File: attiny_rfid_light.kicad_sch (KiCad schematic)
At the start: 27 parts, among them IC1 EM4095, U1 ESP32-WROOM-32, U2 NCP1117-3.3_SOT223

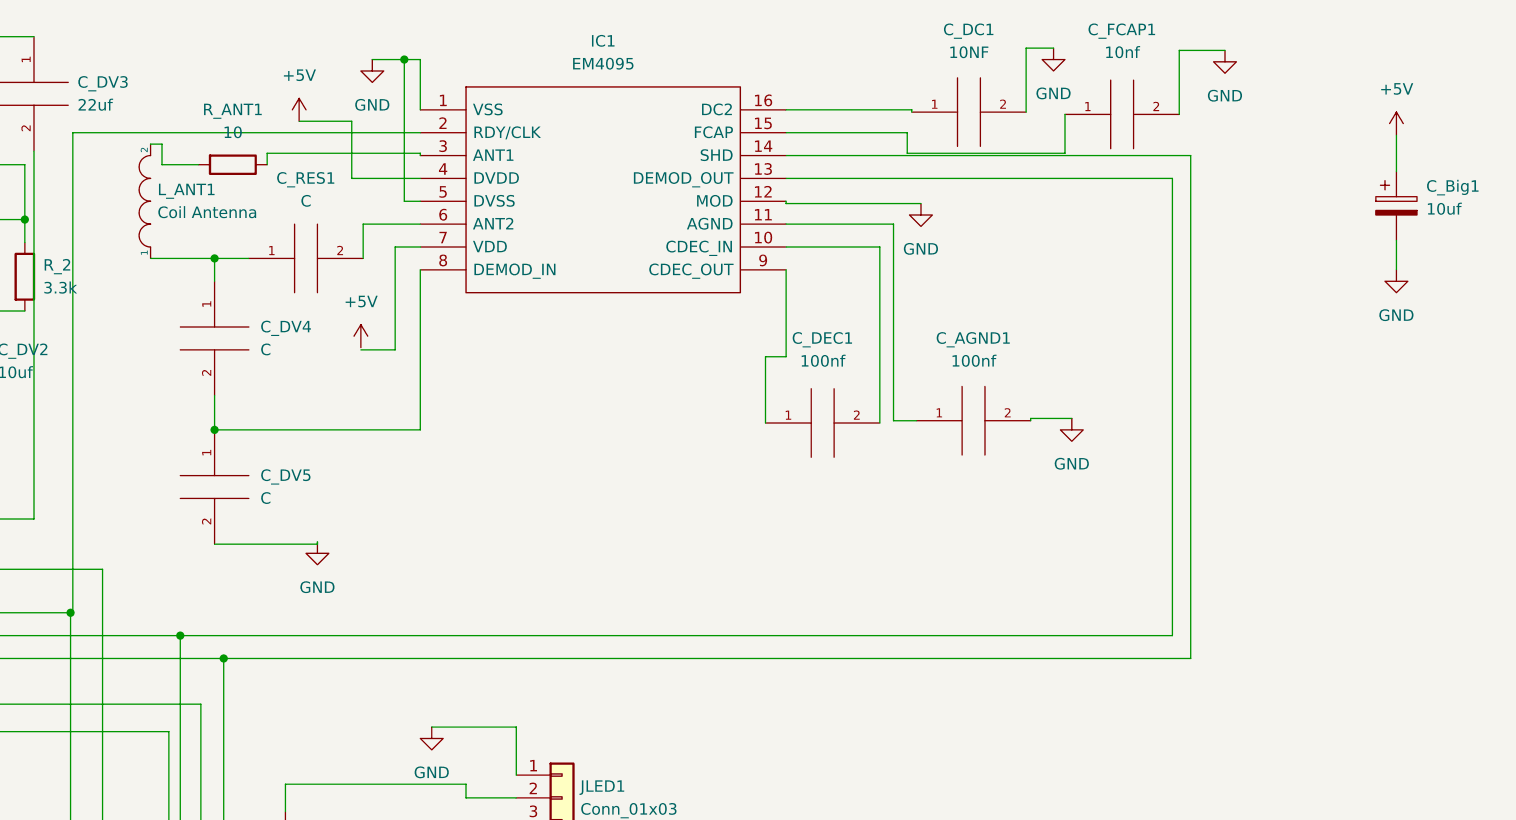
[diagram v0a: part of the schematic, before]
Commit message: Update fix antenna direction and missing shd trace
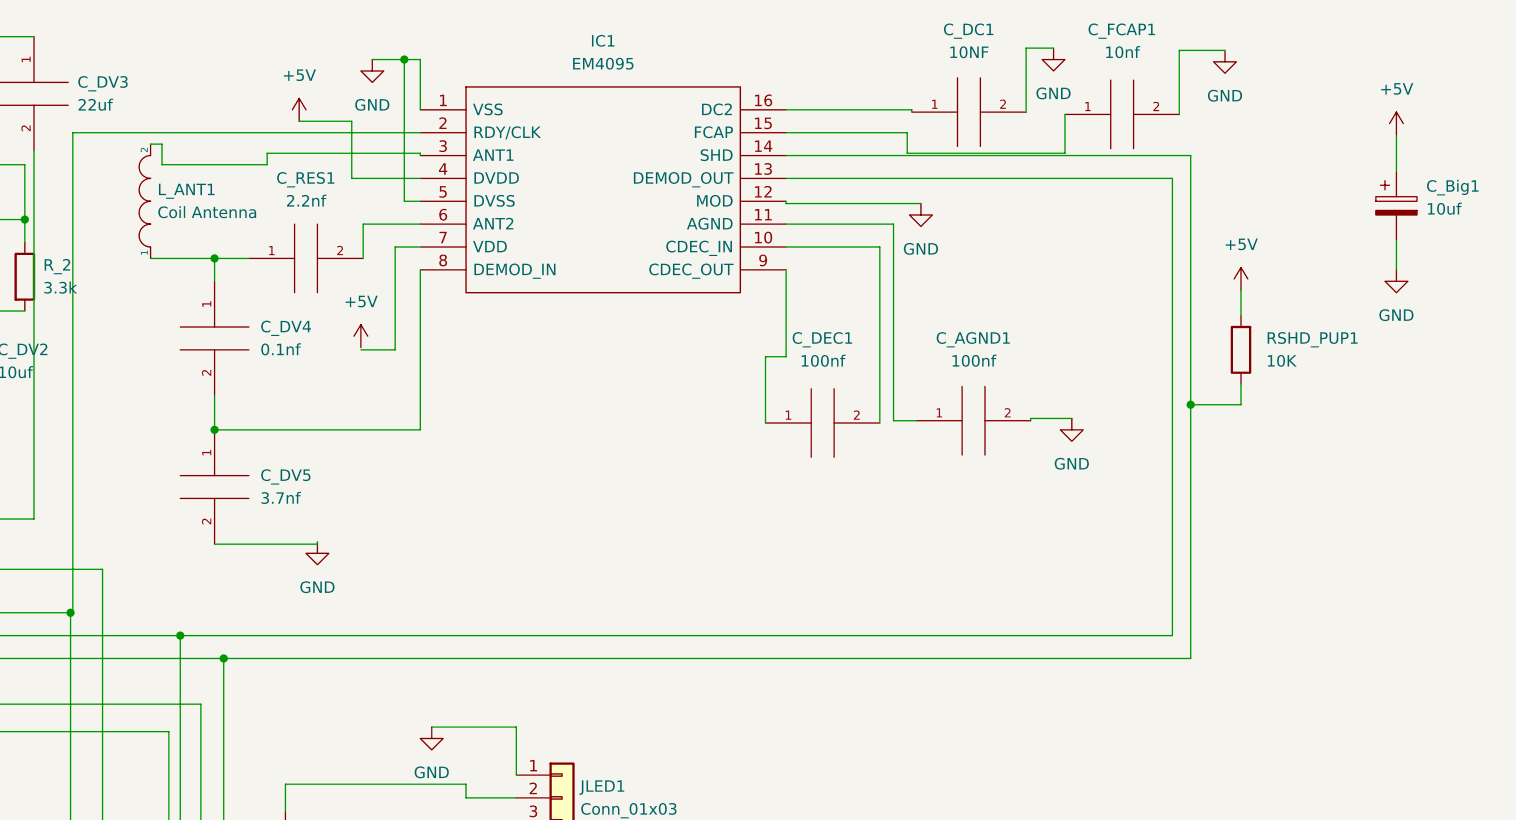
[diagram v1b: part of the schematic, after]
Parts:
- removed R_ANT1: 10, Resistor_SMD:R_0805_2012Metric_Pad1.20x1.40mm_HandSolder, symbol Device:R
- added RSHD_PUP1: 10K, Resistor_SMD:R_0805_2012Metric_Pad1.20x1.40mm_HandSolder, symbol Device:R
- C_DV4: value C -> 0.1nf
- C_DV5: value C -> 3.7nf
- C_RES1: value C -> 2.2nf
- L_ANT1: footprint pcb_inductors:60_turn_square_inductor -> pcb_inductors:60_turn_square_inductor_corrected
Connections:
- net +5V: now also RSHD_PUP1.2
- net at IC1.14 (SHD), J_DEBUG1.4 (Pin_4), U1.26 (IO4): now also RSHD_PUP1.1
- net at IC1.3 (ANT1): now also L_ANT1.2
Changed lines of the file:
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@@
   (junction (at 90.17 80.01) (diameter 0) (color 0 0 0 0)
   )
+  (junction (at 202.438 54.356) (diameter 0) (color 0 0 0 0)
+  )
   (junction (at 59.436 41.402) (diameter 0) (color 0 0 0 0)
   )
@@
     (stroke (width 0) (type default) (color 0 0 0 0))
   )
+  (wire (pts (xy 208.026 41.656) (xy 208.026 44.45))
+    (stroke (width 0) (type default) (color 0 0 0 0))
+  )
   (wire (pts (xy 170.942 26.416) (xy 188.468 26.416))
     (stroke (width 0) (type default) (color 0 0 0 0))
@@
     (stroke (width 0) (type default) (color 0 0 0 0))
   )
+  (wire (pts (xy 208.026 54.356) (xy 202.438 54.356))
+    (stroke (width 0) (type default) (color 0 0 0 0))
+  )
   (wire (pts (xy 116.84 26.416) (xy 116.84 26.67))
     (stroke (width 0) (type default) (color 0 0 0 0))
@@
     (stroke (width 0) (type default) (color 0 0 0 0))
   )
+  (wire (pts (xy 202.438 54.356) (xy 202.438 26.67))
+    (stroke (width 0) (type default) (color 0 0 0 0))
+  )
   (wire (pts (xy 121.92 98.044) (xy 127.508 98.044))
     (stroke (width 0) (type default) (color 0 0 0 0))
@@
     (stroke (width 0) (type default) (color 0 0 0 0))
   )
-  (wire (pts (xy 92.202 27.686) (xy 88.138 27.686))
+  (wire (pts (xy 208.026 52.07) (xy 208.026 54.356))
+    (stroke (width 0) (type default) (color 0 0 0 0))
+  )
+  (wire (pts (xy 88.138 27.686) (xy 99.822 27.686))
     (stroke (width 0) (type default) (color 0 0 0 0))
   )
@@
     (stroke (width 0) (type default) (color 0 0 0 0))
   )
-  (wire (pts (xy 202.438 82.55) (xy 202.438 26.67))
+  (wire (pts (xy 202.438 82.55) (xy 202.438 54.356))
     (stroke (width 0) (type default) (color 0 0 0 0))
   )
@@
       (effects (font (size 1.27 1.27)) (justify left))
     )
-    (property "Value" "C" (id 1) (at 99.06 64.7699 0)
+    (property "Value" "3.7nf" (id 1) (at 99.06 64.7699 0)
       (effects (font (size 1.27 1.27)) (justify left))
     )
@@
   (symbol (lib_id "power:+5V") (at 225.298 24.384 0) (unit 1)
     (in_bom yes) (on_board yes) (fields_autoplaced)
-    (property "Reference" "#PWR019" (id 0) (at 225.298 28.194 0)
+    (property "Reference" "#PWR020" (id 0) (at 225.298 28.194 0)
       (effects (font (size 1.27 1.27)) hide)
     )
@@
     )
     (pin "1")
-  )
-  (symbol (lib_id "Device:R") (at 96.012 27.686 270) (unit 1)
-    (in_bom yes) (on_board yes) (fields_autoplaced)
-    (property "Reference" "R_ANT1" (id 0) (at 96.012 21.59 90))
-    (property "Value" "10" (id 1) (at 96.012 24.13 90))
-    (property "Footprint" "Resistor_SMD:R_0805_2012Metric_Pad1.20x1.40mm_HandSolder" (id 2) (at 96.012 25.908 90)
-      (effects (font (size 1.27 1.27)) hide)
-    )
-    (property "Datasheet" "~" (id 3) (at 96.012 27.686 0)
-      (effects (font (size 1.27 1.27)) hide)
-    )
-    (pin "1")
-    (pin "2")
   )
   (symbol (lib_id "power:GND") (at 118.11 90.17 0) (unit 1)
@@
     (pin "1")
   )
+  (symbol (lib_id "Device:R") (at 208.026 48.26 180) (unit 1)
+    (in_bom yes) (on_board yes) (fields_autoplaced)
+    (property "Reference" "RSHD_PUP1" (id 0) (at 210.82 46.9899 0)
+      (effects (font (size 1.27 1.27)) (justify right))
+    )
+    (property "Value" "10K" (id 1) (at 210.82 49.5299 0)
+      (effects (font (size 1.27 1.27)) (justify right))
+    )
+    (property "Footprint" "Resistor_SMD:R_0805_2012Metric_Pad1.20x1.40mm_HandSolder" (id 2) (at 209.804 48.26 90)
+      (effects (font (size 1.27 1.27)) hide)
+    )
+    (property "Datasheet" "~" (id 3) (at 208.026 48.26 0)
+      (effects (font (size 1.27 1.27)) hide)
+    )
+    (pin "1")
+    (pin "2")
+  )
   (symbol (lib_id "power:GND") (at 172.466 32.004 0) (unit 1)
     (in_bom yes) (on_board yes) (fields_autoplaced)
@@
       (effects (font (size 1.27 1.27)) (justify left))
     )
-    (property "Value" "C" (id 1) (at 99.06 48.2599 0)
+    (property "Value" "0.1nf" (id 1) (at 99.06 48.2599 0)
       (effects (font (size 1.27 1.27)) (justify left))
     )
@@
   (symbol (lib_id "power:GND") (at 225.298 39.37 0) (unit 1)
     (in_bom yes) (on_board yes) (fields_autoplaced)
-    (property "Reference" "#PWR020" (id 0) (at 225.298 45.72 0)
+    (property "Reference" "#PWR021" (id 0) (at 225.298 45.72 0)
       (effects (font (size 1.27 1.27)) hide)
     )
@@
     (pin "1")
   )
+  (symbol (lib_id "power:+5V") (at 208.026 41.656 0) (unit 1)
+    (in_bom yes) (on_board yes) (fields_autoplaced)
+    (property "Reference" "#PWR019" (id 0) (at 208.026 45.466 0)
+      (effects (font (size 1.27 1.27)) hide)
+    )
+    (property "Value" "+5V" (id 1) (at 208.026 36.576 0))
+    (property "Footprint" "" (id 2) (at 208.026 41.656 0)
+      (effects (font (size 1.27 1.27)) hide)
+    )
+    (property "Datasheet" "" (id 3) (at 208.026 41.656 0)
+      (effects (font (size 1.27 1.27)) hide)
+    )
+    (pin "1")
+  )
   (symbol (lib_id "pspice:C") (at 47.498 40.386 0) (unit 1)
     (in_bom yes) (on_board yes) (fields_autoplaced)
@@
       (effects (font (size 1.27 1.27)) (justify right))
     )
-    (property "Footprint" "pcb_inductors:60_turn_square_inductor" (id 2) (at 86.868 31.75 0)
+    (property "Footprint" "pcb_inductors:60_turn_square_inductor_corrected" (id 2) (at 86.868 31.75 0)
       (effects (font (size 1.27 1.27)) hide)
     )
@@
     (in_bom yes) (on_board yes) (fields_autoplaced)
     (property "Reference" "C_RES1" (id 0) (at 104.14 29.21 90))
-    (property "Value" "C" (id 1) (at 104.14 31.75 90))
+    (property "Value" "2.2nf" (id 1) (at 104.14 31.75 90))
     (property "Footprint" "Capacitor_SMD:C_0805_2012Metric_Pad1.18x1.45mm_HandSolder" (id 2) (at 104.14 38.1 0)
       (effects (font (size 1.27 1.27)) hide)
@@
       (reference "#PWR018") (unit 1) (value "GND") (footprint "")
     )
+    (path "/b85b5a44-5181-4c70-bb4d-8740fed21aeb"
+      (reference "#PWR019") (unit 1) (value "+5V") (footprint "")
+    )
     (path "/160fdae6-4399-4d83-be6f-257342eb6a1a"
-      (reference "#PWR019") (unit 1) (value "+5V") (footprint "")
+      (reference "#PWR020") (unit 1) (value "+5V") (footprint "")
     )
     (path "/9ce4a190-6d15-4275-9160-36acf534b781"
-      (reference "#PWR020") (unit 1) (value "GND") (footprint "")
+      (reference "#PWR021") (unit 1) (value "GND") (footprint "")
     )
     (path "/fc3bfa78-5d04-417d-b08f-768062b2f9aa"
@@
     )
     (path "/88f84baf-7afe-41aa-824c-29b1057bce53"
-      (reference "C_DV4") (unit 1) (value "C") (footprint "Capacitor_SMD:C_0805_2012Metric_Pad1.18x1.45mm_HandSolder")
+      (reference "C_DV4") (unit 1) (value "0.1nf") (footprint "Capacitor_SMD:C_0805_2012Metric_Pad1.18x1.45mm_HandSolder")
     )
     (path "/0970727f-11dd-473f-b585-f40294eee11b"
-      (reference "C_DV5") (unit 1) (value "C") (footprint "Capacitor_SMD:C_0805_2012Metric_Pad1.18x1.45mm_HandSolder")
+      (reference "C_DV5") (unit 1) (value "3.7nf") (footprint "Capacitor_SMD:C_0805_2012Metric_Pad1.18x1.45mm_HandSolder")
     )
     (path "/5fade6ac-277b-43df-8e3a-ea7ae9efe0a9"
@@
     )
     (path "/eb36eec3-209f-45cf-a105-18a7e7672fef"
-      (reference "C_RES1") (unit 1) (value "C") (footprint "Capacitor_SMD:C_0805_2012Metric_Pad1.18x1.45mm_HandSolder")
+      (reference "C_RES1") (unit 1) (value "2.2nf") (footprint "Capacitor_SMD:C_0805_2012Metric_Pad1.18x1.45mm_HandSolder")
     )
     (path "/72ff0485-f700-4243-a66c-13414af86c8f"
@@
     )
     (path "/c4f366cf-8726-47ee-87f5-b5abbd410713"
-      (reference "L_ANT1") (unit 1) (value "Coil Antenna") (footprint "pcb_inductors:60_turn_square_inductor")
+      (reference "L_ANT1") (unit 1) (value "Coil Antenna") (footprint "pcb_inductors:60_turn_square_inductor_corrected")
+    )
+    (path "/81c65984-9f9d-492c-82f9-bbe24b88ebc2"
+      (reference "RSHD_PUP1") (unit 1) (value "10K") (footprint "Resistor_SMD:R_0805_2012Metric_Pad1.20x1.40mm_HandSolder")
     )
     (path "/b2b8605e-6475-43cb-8fde-09cbdf493df9"
@@
       (reference "R_5") (unit 1) (value "490") (footprint "Resistor_SMD:R_0805_2012Metric_Pad1.20x1.40mm_HandSolder")
     )
-    (path "/44969654-d9c0-4162-a4de-27f40e0edb65"
-      (reference "R_ANT1") (unit 1) (value "10") (footprint "Resistor_SMD:R_0805_2012Metric_Pad1.20x1.40mm_HandSolder")
-    )
     (path "/dd8613f5-26c5-442c-934d-db0fe188f421"

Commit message: v3
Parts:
- removed C1: 100uf, Capacitor_SMD:C_0805_2012Metric_Pad1.18x1.45mm_HandSolder, symbol pspice:C
- removed C_DV2: 10uf, Capacitor_SMD:C_0805_2012Metric_Pad1.18x1.45mm_HandSolder, symbol pspice:C
- removed R_2: 3.3k, Resistor_SMD:R_0805_2012Metric_Pad1.20x1.40mm_HandSolder, symbol Device:R
- added C_DV4: 3.7nf split between 2, Capacitor_SMD:C_0805_2012Metric_Pad1.18x1.45mm_HandSolder, symbol pspice:C
- added C_RESOptional1: NA, Capacitor_SMD:C_0805_2012Metric_Pad1.18x1.45mm_HandSolder, symbol pspice:C
- C_Big1: value 10uf -> 100uf
- C_DV2: renamed from C_DV3; value 22uf -> 10uf
- C_DV5: value 3.7nf -> 3.7nf split between 2
- R_2: renamed from R_3; value 5k -> 5k1 or 5k? was 5k og
- R_4: value 5k -> 5k1 og was 5k
- renumbered C2 to C1, C3 to C2, C_DV4 to C_DV3, R_5 to R_3
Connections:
- net +3V3: now also C_DV2.1, J_DEBUG1.2 (Pin_2), U2.2 (VO); no longer J_DEBUG1.1 (Pin_1), J_DEBUG1.7 (Pin_7)
- net +5V: now also IC1.7 (VDD), J_DEBUG1.3 (Pin_3)
- net GND: now also J_DEBUG1.1 (Pin_1), C_DV4.2
- net at IC1.2 (RDY/CLK), U1.23 (IO15): no longer J_DEBUG1.2 (Pin_2)
- net at IC1.13 (DEMOD_OUT), U1.27 (IO16): no longer J_DEBUG1.3 (Pin_3)
- net at IC1.14 (SHD), RSHD_PUP1.1, U1.26 (IO4): no longer J_DEBUG1.4 (Pin_4)
- net at C_DV3.2, C_DV5.1, IC1.8 (DEMOD_IN): now also C_DV4.1
- net at C_RES1.2, IC1.6 (ANT2): now also C_RESOptional1.2
- net at C_DV3.1, C_RES1.1, L_ANT1.1: now also C_RESOptional1.1
- net at JLED1.2 (Pin_2): now also R_3.1; no longer R_3.2
- net at U1.13 (IO14): now also R_3.2; no longer R_3.1
- net at R_2.2, U1.25 (IO0): now also J_DEBUG1.7 (Pin_7)
- net at U1.29 (IO5): now also J_DEBUG1.4 (Pin_4)
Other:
- moved on the sheet: C_AGND1, C_Big1, C_DC1, C_DEC1, C_DV2, C_DV3, C_DV5, C_FCAP1, C_RES1, IC1, JLED1, L_ANT1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
